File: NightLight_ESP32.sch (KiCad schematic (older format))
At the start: 25 parts, among them J1 USB_OTG, J2 BUTTON, Q1 MMBT2222, Q2 MMBT2222, SW1 TL3342, SW2 TL3342, U1 ESP32-WROOM-32D, U2 AP2112K-3.3, U3 CP2104

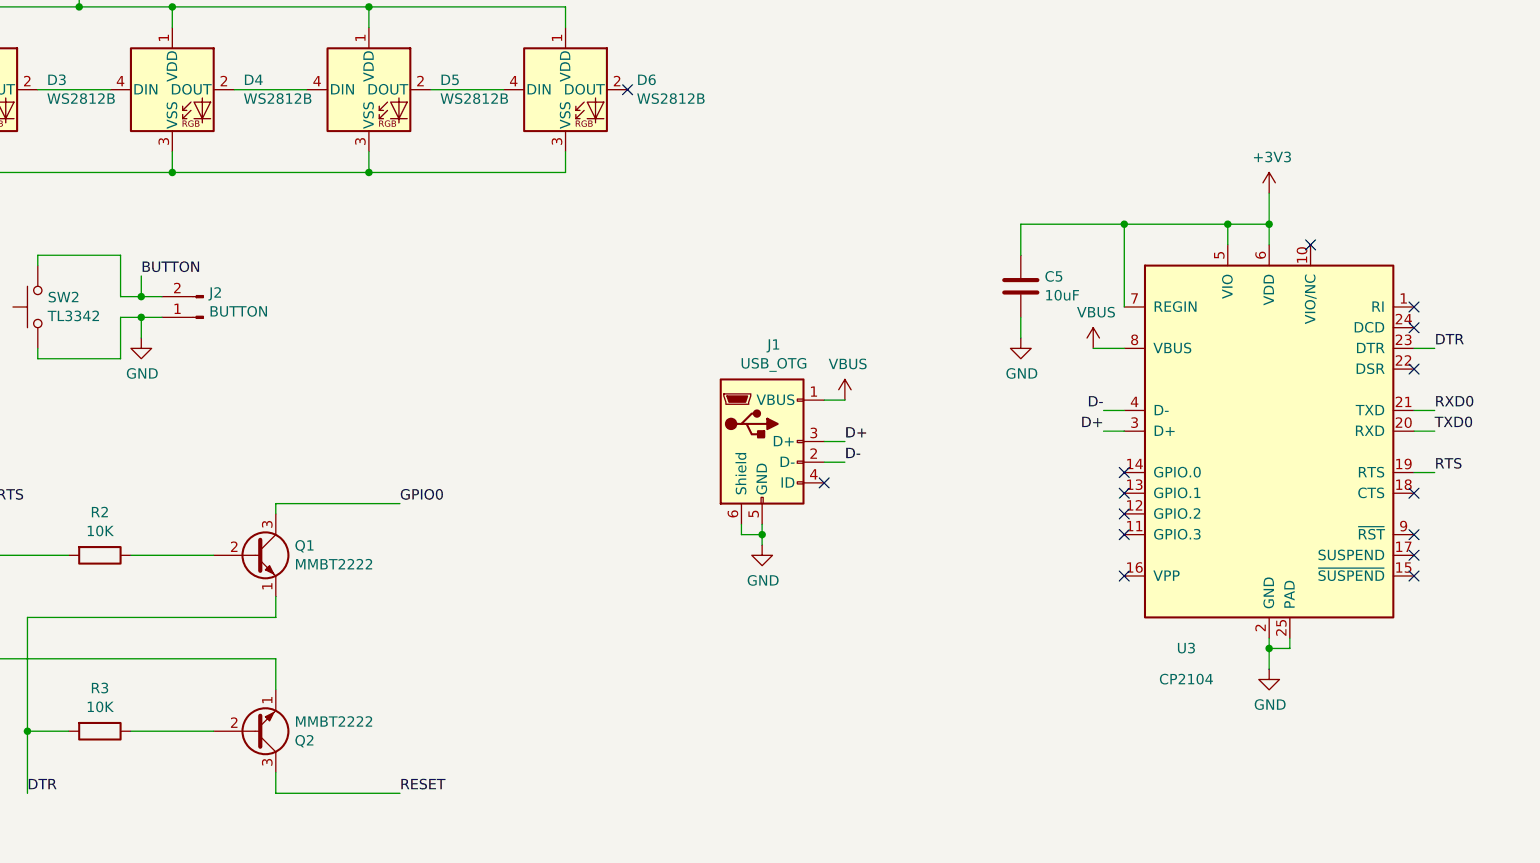
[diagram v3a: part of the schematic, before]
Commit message: Updated to USB C and CH340
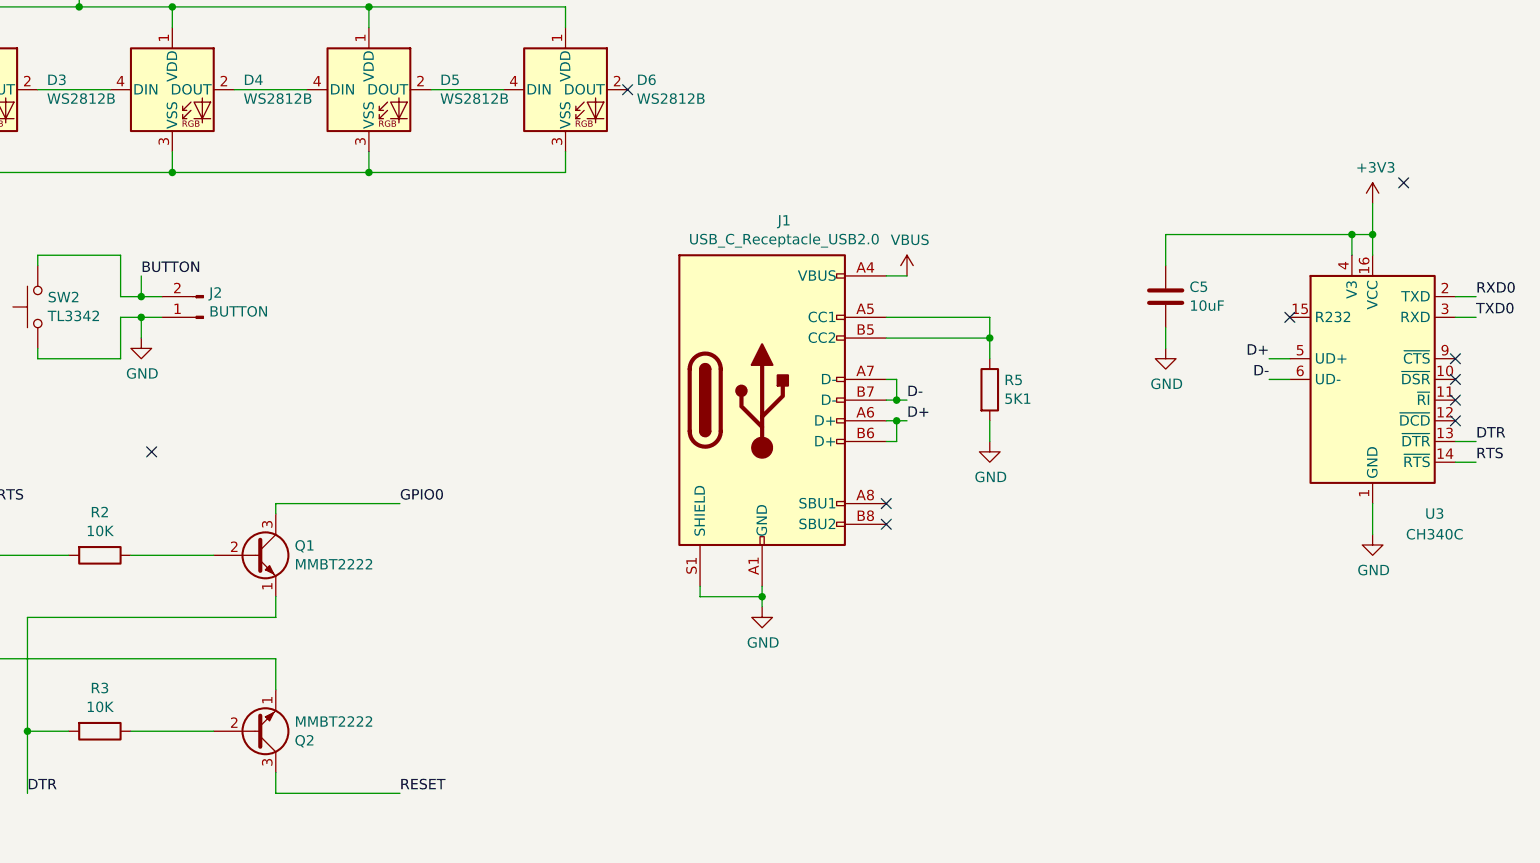
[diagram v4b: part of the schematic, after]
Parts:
- removed J1: USB_OTG, Connector_USB:USB_Micro-B_Amphenol_10103594-0001LF_Horizontal, symbol Connector:USB_OTG
- removed U3: CP2104, Package_DFN_QFN:QFN-24-1EP_4x4mm_P0.5mm_EP2.6x2.6mm, symbol Interface_USB:CP2104
- added J1: USB_C_Receptacle_USB2.0, Connector_USB:USB_C_Receptacle_HRO_TYPE-C-31-M-12, symbol Connector:USB_C_Receptacle_USB2.0
- added R5: 5K1, Resistor_SMD:R_0805_2012Metric, symbol Device:R
- added U3: CH340C, Package_SO:SOIC-16_3.9x9.9mm_P1.27mm, symbol Interface_USB:CH340C
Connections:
- net +3V3: now also U3.16 (VCC), U3.4 (V3)
- net D+: now also J1.A6 (D+), J1.B6 (D+), U3.5 (UD+)
- net D-: now also J1.A7 (D-), J1.B7 (D-), U3.6 (UD-)
- net DTR: now also U3.13 (~DTR)
- net GND: now also J1.A1 (GND), J1.A12 (GND), J1.B1 (GND), J1.B12 (GND), J1.S1 (SHIELD), R5.2, U3.1 (GND)
- net RTS: now also U3.14 (~RTS)
- net RXD0: now also U3.2 (TXD)
- net TXD0: now also U3.3 (RXD)
- net VBUS: now also J1.A4 (VBUS), J1.A9 (VBUS), J1.B4 (VBUS), J1.B9 (VBUS)
- new net: J1.A5 (CC1), J1.B5 (CC2), R5.1
- no-connect marks 42 -> 37
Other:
- moved on the sheet: C5

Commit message: Added part corrections
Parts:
- J1: JLCPCB_CORRECTION (none) -> 1.8;-0.3;180
- R5: LCSC (none) -> C139928
- U3: JLCPCB_CORRECTION (none) -> 0;0;90
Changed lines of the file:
@@
 F 3 "https://datasheet.lcsc.com/szlcsc/Jiangsu-Qin-Heng-CH340C_C84681.pdf" H 9900 5500 50  0001 C CNN
 F 4 "C84681" H 10250 4700 50  0001 C CNN "LCSC"
+F 5 "0;0;90" H 10250 4700 50  0001 C CNN "JLCPCB_CORRECTION"
 	1    10250 4700
 	1    0    0    -1
@@
 F 2 "Resistor_SMD:R_0805_2012Metric" V 8330 4750 50  0001 C CNN
 F 3 "~" H 8400 4750 50  0001 C CNN
+F 4 "C139928" H 8400 4750 50  0001 C CNN "LCSC"
 	1    8400 4750
 	1    0    0    -1
@@
 F 3 "https://www.usb.org/sites/default/files/documents/usb_type-c.zip" H 7450 4800 50  0001 C CNN
 F 4 "C165948" H 7300 4800 50  0001 C CNN "LCSC"
+F 5 "1.8;-0.3;180" H 7300 4800 50  0001 C CNN "JLCPCB_CORRECTION"
 	1    7300 4800
 	1    0    0    -1

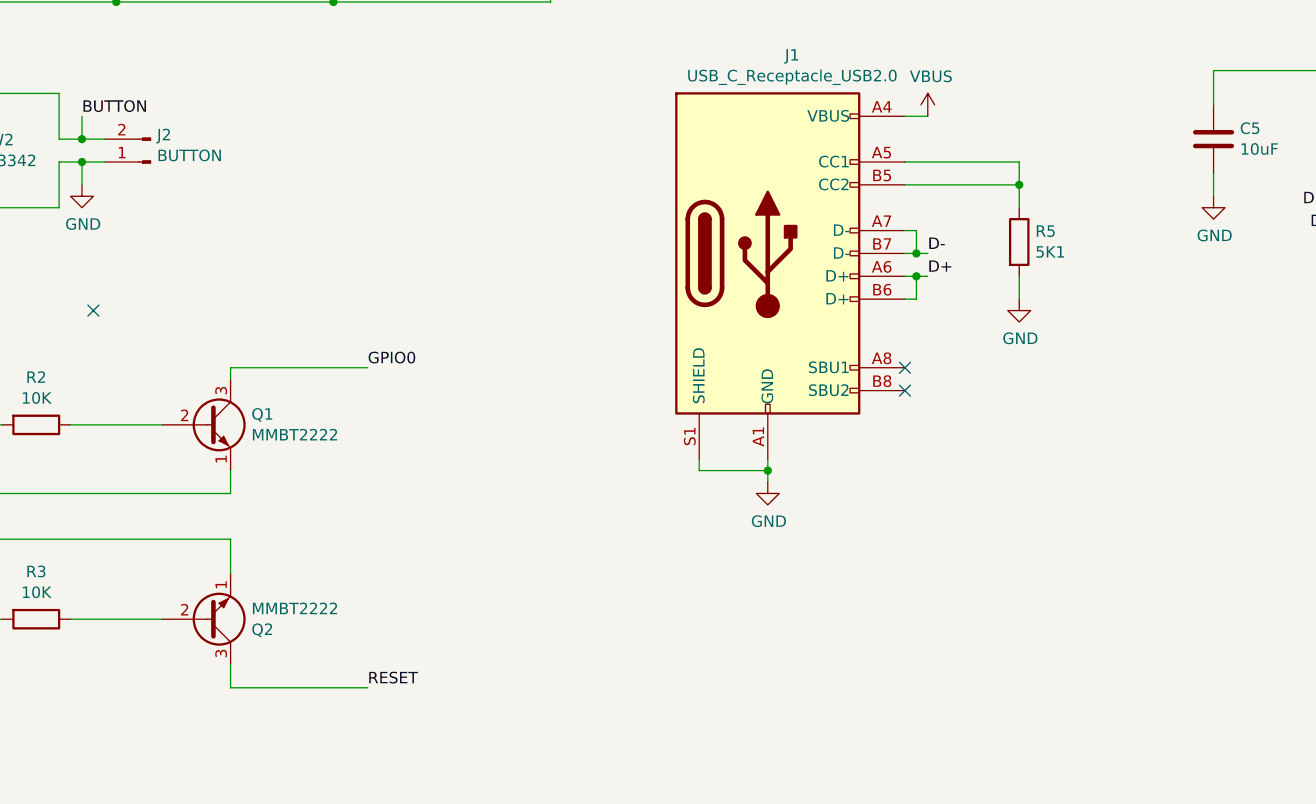
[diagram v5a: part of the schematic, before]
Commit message: Fix issue with USB C CC1/CC2 needing two resistors and the wrong schematic symbol for the MMBT2222, leading to the wrong pinout
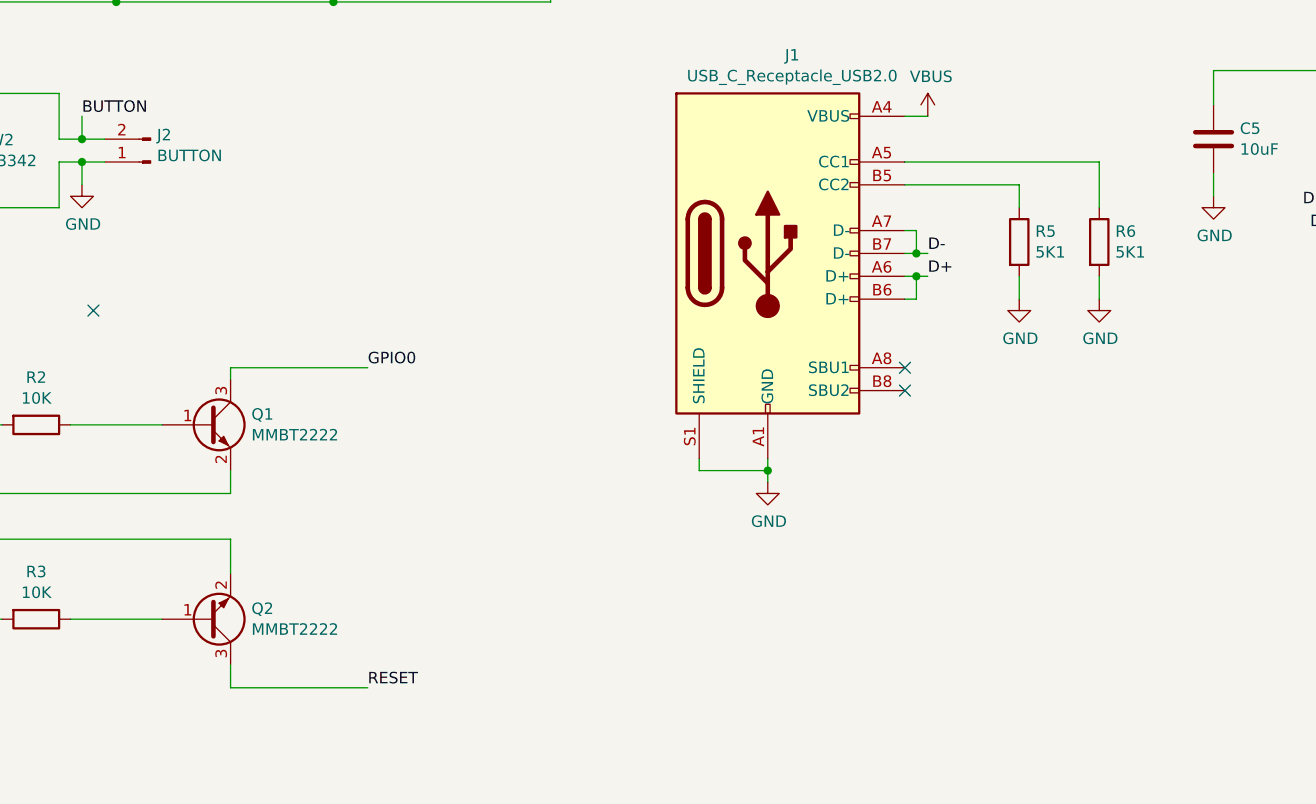
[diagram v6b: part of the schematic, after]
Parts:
- removed Q1, Q2: MMBT2222, Package_TO_SOT_SMD:SOT-23, symbol Transistor_BJT:S8050
- added Q1, Q2: MMBT2222, Package_TO_SOT_SMD:SOT-23, symbol Transistor_BJT:MMBT3904
- added R6: 5K1, Resistor_SMD:R_0805_2012Metric, symbol Device:R
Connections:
- net DTR: now also Q1.2 (E)
- net GND: now also R6.2
- net GPIO0: now also Q1.3 (C)
- net RESET: now also Q2.3 (C)
- net RTS: now also Q2.2 (E)
- net at R2.1: now also Q1.1 (B)
- net at R3.1: now also Q2.1 (B)
- net at J1.B5 (CC2), R5.1: no longer J1.A5 (CC1)
- new net: J1.A5 (CC1), R6.1
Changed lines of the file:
@@
 Title "SmartishNight"
 Date "2020-11-03"
-Rev "1"
+Rev "1.2"
 Comp ""
 Comment1 ""
@@
 	1    4450 3300
 	1    0    0    -1
-$EndComp
-$Comp
-L Transistor_BJT:S8050 Q1
-U 1 1 5F9FAC23
-P 4850 5550
-F 0 "Q1" H 5041 5596 50  0000 L CNN
-F 1 "MMBT2222" H 5041 5505 50  0000 L CNN
-F 2 "Package_TO_SOT_SMD:SOT-23" H 5050 5475 50  0001 L CIN
-F 3 "http://www.unisonic.com.tw/datasheet/S8050.pdf" H 4850 5550 50  0001 L CNN
-F 4 "C181121" H 4850 5550 50  0001 C CNN "LCSC"
-F 5 "0;0;180" H 4850 5550 50  0001 C CNN "JLCPCB_CORRECTION"
-	1    4850 5550
-	1    0    0    -1
-$EndComp
-$Comp
-L Transistor_BJT:S8050 Q2
-U 1 1 5F9FB2FD
-P 4850 6400
-F 0 "Q2" H 5041 6446 50  0000 L CNN
-F 1 "MMBT2222" H 5041 6355 50  0000 L CNN
-F 2 "Package_TO_SOT_SMD:SOT-23" H 5050 6325 50  0001 L CIN
-F 3 "http://www.unisonic.com.tw/datasheet/S8050.pdf" H 4850 6400 50  0001 L CNN
-F 4 "C181121" H 4850 6400 50  0001 C CNN "LCSC"
-F 5 "0;0;180" H 4850 6400 50  0001 C CNN "JLCPCB_CORRECTION"
-	1    4850 6400
-	1    0    0    1
 $EndComp
 $Comp
@@
 	8400 4500 8400 4600
 Wire Wire Line
-	7900 4400 8400 4400
-Wire Wire Line
-	8400 4400 8400 4500
-Connection ~ 8400 4500
-Wire Wire Line
 	8400 4900 8400 5000
 NoConn ~ 7900 5300
@@
 	1    0    0    -1
 $EndComp
+$Comp
+L Device:R R6
+U 1 1 60D03576
+P 8750 4750
+F 0 "R6" H 8820 4796 50  0000 L CNN
+F 1 "5K1" H 8820 4705 50  0000 L CNN
+F 2 "Resistor_SMD:R_0805_2012Metric" V 8680 4750 50  0001 C CNN
+F 3 "~" H 8750 4750 50  0001 C CNN
+F 4 "C139928" H 8750 4750 50  0001 C CNN "LCSC"
+	1    8750 4750
+	1    0    0    -1
+$EndComp
+$Comp
+L power:GND #PWR0118
+U 1 1 60D03BEA
+P 8750 5000
+F 0 "#PWR0118" H 8750 4750 50  0001 C CNN
+F 1 "GND" H 8755 4827 50  0000 C CNN
+F 2 "" H 8750 5000 50  0001 C CNN
+F 3 "" H 8750 5000 50  0001 C CNN
+	1    8750 5000
+	1    0    0    -1
+$EndComp
+Wire Wire Line
+	8750 4900 8750 5000
+Wire Wire Line
+	8750 4600 8750 4400
+Wire Wire Line
+	8750 4400 7900 4400
+$Comp
+L Transistor_BJT:MMBT3904 Q1
+U 1 1 60D158B1
+P 4850 5550
+F 0 "Q1" H 5041 5596 50  0000 L CNN
+F 1 "MMBT2222" H 5041 5505 50  0000 L CNN
+F 2 "Package_TO_SOT_SMD:SOT-23" H 5050 5475 50  0001 L CIN
+F 3 "https://www.onsemi.com/pub/Collateral/2N3903-D.PDF" H 4850 5550 50  0001 L CNN
+	1    4850 5550
+	1    0    0    -1
+$EndComp
+$Comp
+L Transistor_BJT:MMBT3904 Q2
+U 1 1 60D21C89
+P 4850 6400
+F 0 "Q2" H 5041 6354 50  0000 L CNN
+F 1 "MMBT2222" H 5041 6445 50  0000 L CNN
+F 2 "Package_TO_SOT_SMD:SOT-23" H 5050 6325 50  0001 L CIN
+F 3 "https://www.onsemi.com/pub/Collateral/2N3903-D.PDF" H 4850 6400 50  0001 L CNN
+	1    4850 6400
+	1    0    0    1
+$EndComp
 $EndSCHEMATC

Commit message: Corrected part for the USB C power signalling
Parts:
- R5, R6: LCSC C139928 -> C27834
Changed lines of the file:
@@
 F 2 "Resistor_SMD:R_0805_2012Metric" V 8330 4750 50  0001 C CNN
 F 3 "~" H 8400 4750 50  0001 C CNN
-F 4 "C139928" H 8400 4750 50  0001 C CNN "LCSC"
+F 4 "C27834" H 8400 4750 50  0001 C CNN "LCSC"
 	1    8400 4750
 	1    0    0    -1
@@
 F 2 "Resistor_SMD:R_0805_2012Metric" V 8680 4750 50  0001 C CNN
 F 3 "~" H 8750 4750 50  0001 C CNN
-F 4 "C139928" H 8750 4750 50  0001 C CNN "LCSC"
+F 4 "C27834" H 8750 4750 50  0001 C CNN "LCSC"
 	1    8750 4750
 	1    0    0    -1
